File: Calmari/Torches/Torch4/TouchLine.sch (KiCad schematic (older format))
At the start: 18 parts

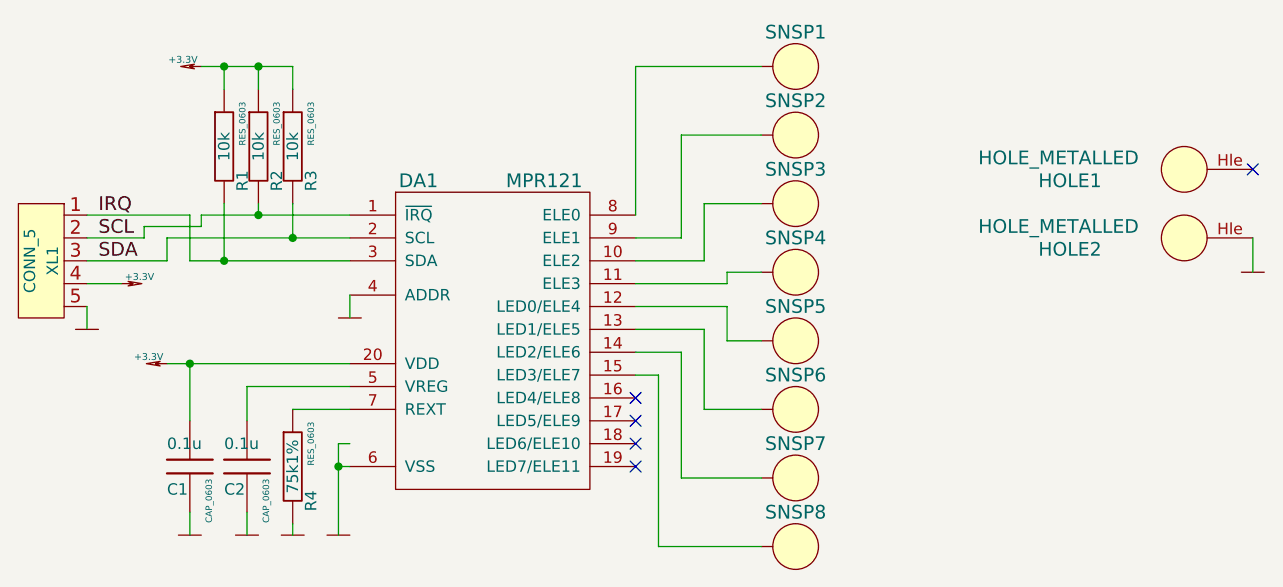
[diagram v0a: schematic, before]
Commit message: 
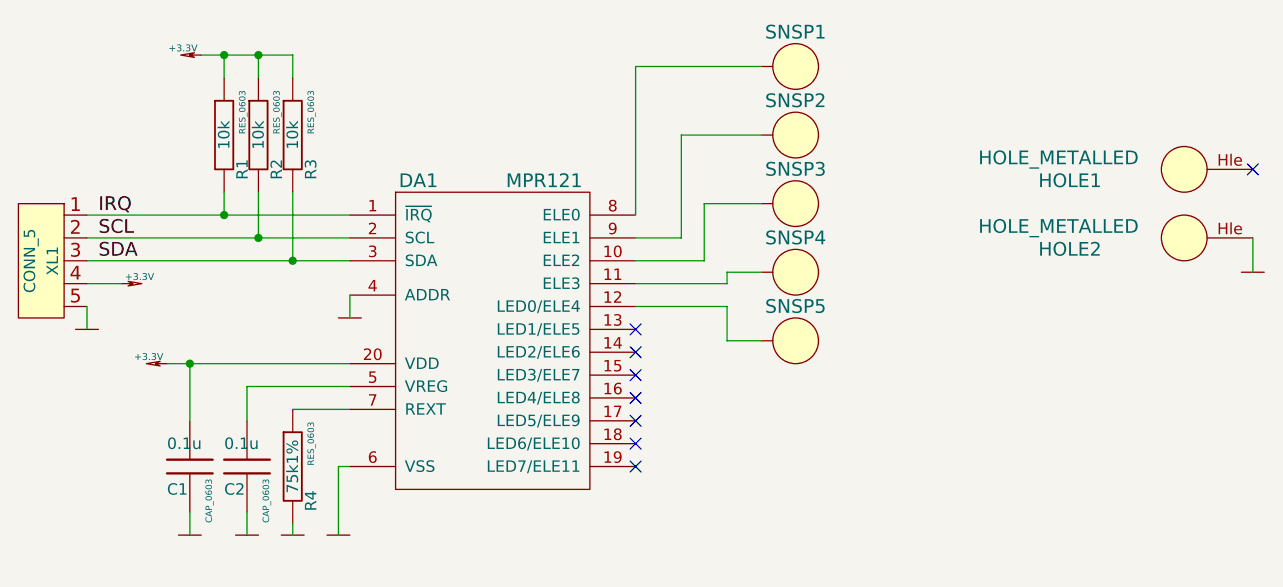
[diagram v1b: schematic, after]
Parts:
- removed SNSP6, SNSP7, SNSP8: SENSORPAD, symbol SENSORPAD
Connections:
- net IRQ: now also DA1.1 (~IRQ); no longer DA1.3 (SDA)
- net SCL: now also DA1.2 (SCL); no longer DA1.1 (~IRQ)
- net SDA: now also DA1.3 (SDA); no longer DA1.2 (SCL)
- no-connect marks 5 -> 8
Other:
- moved on the sheet: R1, R2, R3
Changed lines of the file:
@@
 LIBS:Sensors
 LIBS:Tittar_kl
+LIBS:TouchLine-cache
 EELAYER 27 0
 EELAYER END
@@
 Sheet 1 1
 Title ""
-Date "1 sep 2014"
+Date "15 sep 2014"
 Rev ""
 Comp ""
@@
 L R R3
 U 1 1 54045D60
-P 4750 2400
-F 0 "R3" V 4830 2250 50  0000 C CNN
-F 1 "10k" V 4750 2400 50  0000 C CNN
-F 2 "RES_0603" V 4830 2500 28  0000 C CNN
-F 3 "~" H 4750 2400 60  0000 C CNN
-	1    4750 2400
+P 4750 2350
+F 0 "R3" V 4830 2200 50  0000 C CNN
+F 1 "10k" V 4750 2350 50  0000 C CNN
+F 2 "RES_0603" V 4830 2450 28  0000 C CNN
+F 3 "~" H 4750 2350 60  0000 C CNN
+	1    4750 2350
 	1    0    0    -1
 $EndComp
@@
 L R R2
 U 1 1 54045D81
-P 4600 2400
-F 0 "R2" V 4680 2250 50  0000 C CNN
-F 1 "10k" V 4600 2400 50  0000 C CNN
-F 2 "RES_0603" V 4680 2500 28  0000 C CNN
-F 3 "~" H 4600 2400 60  0000 C CNN
-	1    4600 2400
+P 4600 2350
+F 0 "R2" V 4680 2200 50  0000 C CNN
+F 1 "10k" V 4600 2350 50  0000 C CNN
+F 2 "RES_0603" V 4680 2450 28  0000 C CNN
+F 3 "~" H 4600 2350 60  0000 C CNN
+	1    4600 2350
 	1    0    0    -1
 $EndComp
@@
 L R R1
 U 1 1 54045D87
-P 4450 2400
-F 0 "R1" V 4530 2250 50  0000 C CNN
-F 1 "10k" V 4450 2400 50  0000 C CNN
-F 2 "RES_0603" V 4530 2500 28  0000 C CNN
-F 3 "~" H 4450 2400 60  0000 C CNN
-	1    4450 2400
+P 4450 2350
+F 0 "R1" V 4530 2200 50  0000 C CNN
+F 1 "10k" V 4450 2350 50  0000 C CNN
+F 2 "RES_0603" V 4530 2450 28  0000 C CNN
+F 3 "~" H 4450 2350 60  0000 C CNN
+	1    4450 2350
 	1    0    0    -1
 $EndComp
@@
 L +3.3V #PWR07
 U 1 1 54045E06
-P 4350 2050
-F 0 "#PWR07" H 4350 2010 30  0001 C CNN
-F 1 "+3.3V" H 4430 2080 30  0000 C CNN
-F 2 "~" H 4350 2050 60  0000 C CNN
-F 3 "~" H 4350 2050 60  0000 C CNN
-	1    4350 2050
+P 4350 2000
+F 0 "#PWR07" H 4350 1960 30  0001 C CNN
+F 1 "+3.3V" H 4430 2030 30  0000 C CNN
+F 2 "~" H 4350 2000 60  0000 C CNN
+F 3 "~" H 4350 2000 60  0000 C CNN
+	1    4350 2000
 	-1   0    0    -1
 $EndComp
@@
 NoConn ~ 6250 3500
 $Comp
-L SENSORPAD SNSP5
-U 1 1 540461E0
-P 6950 3250
-F 0 "SNSP5" H 6950 3400 60  0000 C CNN
-F 1 "SENSORPAD" H 6925 3475 60  0001 C CNN
-F 2 "" H 6950 3250 60  0000 C CNN
-F 3 "" H 6950 3250 60  0000 C CNN
-	1    6950 3250
-	1    0    0    -1
-$EndComp
-$Comp
 L SENSORPAD SNSP4
 U 1 1 540461EF
@@
 $EndComp
 $Comp
-L SENSORPAD SNSP6
-U 1 1 5404620D
-P 6950 3550
-F 0 "SNSP6" H 6950 3700 60  0000 C CNN
-F 1 "SENSORPAD" H 6925 3775 60  0001 C CNN
-F 2 "" H 6950 3550 60  0000 C CNN
-F 3 "" H 6950 3550 60  0000 C CNN
-	1    6950 3550
-	1    0    0    -1
-$EndComp
-$Comp
 L SENSORPAD SNSP2
 U 1 1 5404621C
@@
 $EndComp
 $Comp
-L SENSORPAD SNSP7
-U 1 1 5404622B
-P 6950 3850
-F 0 "SNSP7" H 6950 4000 60  0000 C CNN
-F 1 "SENSORPAD" H 6925 4075 60  0001 C CNN
-F 2 "" H 6950 3850 60  0000 C CNN
-F 3 "" H 6950 3850 60  0000 C CNN
-	1    6950 3850
-	1    0    0    -1
-$EndComp
-$Comp
 L SENSORPAD SNSP1
 U 1 1 5404623A
@@
 $EndComp
 $Comp
-L SENSORPAD SNSP8
-U 1 1 54046249
-P 6950 4150
-F 0 "SNSP8" H 6950 4300 60  0000 C CNN
-F 1 "SENSORPAD" H 6925 4375 60  0001 C CNN
-F 2 "" H 6950 4150 60  0000 C CNN
-F 3 "" H 6950 4150 60  0000 C CNN
-	1    6950 4150
-	1    0    0    -1
-$EndComp
-$Comp
 L HOLE_METALLED HOLE1
 U 1 1 54047142
@@
 	1    0    0    -1
 $EndComp
-Wire Wire Line
-	4550 4100 4550 4000
-Wire Wire Line
-	4300 4100 4300 4000
-Wire Wire Line
-	4750 4050 4750 4100
-Wire Wire Line
-	4950 4100 4950 3700
-Wire Wire Line
-	4950 3700 5000 3700
-Wire Wire Line
-	5000 3800 4950 3800
-Connection ~ 4950 3800
-Wire Wire Line
-	4750 3550 5000 3550
-Wire Wire Line
-	5000 3450 4550 3450
-Wire Wire Line
-	4550 3450 4550 3600
-Wire Wire Line
-	4200 3350 5000 3350
-Wire Wire Line
-	4300 3350 4300 3600
-Connection ~ 4300 3350
-Wire Wire Line
-	5000 3150 5000 3050
-Wire Wire Line
-	4450 2150 4450 2050
-Wire Wire Line
-	4350 2050 4750 2050
-Wire Wire Line
-	4750 2050 4750 2150
-Wire Wire Line
-	4600 2150 4600 2050
-Connection ~ 4600 2050
-Connection ~ 4450 2050
-Wire Wire Line
-	3850 3200 3850 3100
-Wire Wire Line
-	3850 3000 4000 3000
-Wire Wire Line
-	6250 3000 6650 3000
-Wire Wire Line
-	6650 3000 6650 2950
-Wire Wire Line
-	6650 2950 6800 2950
-Wire Wire Line
-	6250 3100 6650 3100
-Wire Wire Line
-	6650 3100 6650 3250
-Wire Wire Line
-	6650 3250 6800 3250
-Wire Wire Line
-	6250 3200 6550 3200
-Wire Wire Line
-	6550 3200 6550 3550
-Wire Wire Line
-	6550 3550 6800 3550
-Wire Wire Line
-	6250 3300 6450 3300
-Wire Wire Line
-	6450 3300 6450 3850
-Wire Wire Line
-	6450 3850 6800 3850
-Wire Wire Line
-	6250 3400 6350 3400
-Wire Wire Line
-	6350 3400 6350 4150
-Wire Wire Line
-	6350 4150 6800 4150
-Wire Wire Line
-	6250 2900 6550 2900
-Wire Wire Line
-	6550 2900 6550 2650
-Wire Wire Line
-	6550 2650 6800 2650
-Wire Wire Line
-	6250 2800 6450 2800
-Wire Wire Line
-	6450 2800 6450 2350
-Wire Wire Line
-	6450 2350 6800 2350
-Wire Wire Line
-	6250 2700 6250 2050
-Wire Wire Line
-	6250 2050 6800 2050
-Wire Wire Line
-	8950 2950 8950 2800
-Wire Wire Line
-	5000 2900 4300 2900
-Wire Wire Line
-	4300 2900 4300 2700
-Wire Wire Line
-	4300 2700 3850 2700
-Wire Wire Line
-	5000 2800 4200 2800
-Wire Wire Line
-	4200 2800 4200 2900
-Wire Wire Line
-	4200 2900 3850 2900
-Wire Wire Line
-	3850 2800 4100 2800
-Wire Wire Line
-	4100 2800 4100 2750
-Wire Wire Line
-	4100 2750 4350 2750
-Wire Wire Line
-	4350 2750 4350 2700
-Wire Wire Line
-	4350 2700 5000 2700
-Wire Wire Line
-	4450 2650 4450 2900
-Connection ~ 4450 2900
-Wire Wire Line
-	4600 2650 4600 2700
-Connection ~ 4600 2700
-Wire Wire Line
-	4750 2650 4750 2800
-Connection ~ 4750 2800
 Text Label 3900 2700 0    60   ~ 0
 IRQ
@@
 Text Label 3900 2900 0    60   ~ 0
 SDA
+Wire Wire Line
+	4550 4100 4550 4000
+Wire Wire Line
+	4300 4100 4300 4000
+Wire Wire Line
+	4750 4050 4750 4100
+Wire Wire Line
+	5000 3800 4950 3800
+Wire Wire Line
+	4750 3550 5000 3550
+Wire Wire Line
+	5000 3450 4550 3450
+Wire Wire Line
+	4550 3450 4550 3600
+Wire Wire Line
+	4200 3350 5000 3350
+Wire Wire Line
+	4300 3350 4300 3600
+Connection ~ 4300 3350
+Wire Wire Line
+	5000 3150 5000 3050
+Wire Wire Line
+	4450 2100 4450 2000
+Wire Wire Line
+	4350 2000 4750 2000
+Wire Wire Line
+	4750 2000 4750 2100
+Wire Wire Line
+	4600 2100 4600 2000
+Connection ~ 4600 2000
+Connection ~ 4450 2000
+Wire Wire Line
+	3850 3200 3850 3100
+Wire Wire Line
+	3850 3000 4000 3000
+Wire Wire Line
+	6250 3000 6650 3000
+Wire Wire Line
+	6650 3000 6650 2950
+Wire Wire Line
+	6650 2950 6800 2950
+Wire Wire Line
+	6250 2900 6550 2900
+Wire Wire Line
+	6550 2900 6550 2650
+Wire Wire Line
+	6550 2650 6800 2650
+Wire Wire Line
+	6250 2800 6450 2800
+Wire Wire Line
+	6450 2800 6450 2350
+Wire Wire Line
+	6450 2350 6800 2350
+Wire Wire Line
+	6250 2700 6250 2050
+Wire Wire Line
+	6250 2050 6800 2050
+Wire Wire Line
+	8950 2950 8950 2800
+Wire Wire Line
+	3850 2700 5000 2700
+Wire Wire Line
+	3850 2900 5000 2900
+Wire Wire Line
+	3850 2800 5000 2800
+Wire Wire Line
+	4750 2600 4750 2900
+Connection ~ 4750 2900
+Wire Wire Line
+	4600 2600 4600 2800
+Connection ~ 4600 2800
+Wire Wire Line
+	4450 2600 4450 2700
+Connection ~ 4450 2700
+$Comp
+L SENSORPAD SNSP5
+U 1 1 54172112
+P 6950 3250
+F 0 "SNSP5" H 6950 3400 60  0000 C CNN
+F 1 "SENSORPAD" H 6925 3475 60  0001 C CNN
+F 2 "" H 6950 3250 60  0000 C CNN
+F 3 "" H 6950 3250 60  0000 C CNN
+	1    6950 3250
+	1    0    0    -1
+$EndComp
+Wire Wire Line
+	6800 3250 6650 3250
+Wire Wire Line
+	6650 3250 6650 3100
+Wire Wire Line
+	6650 3100 6250 3100
+NoConn ~ 6250 3200
+NoConn ~ 6250 3300
+NoConn ~ 6250 3400
+Wire Wire Line
+	4950 3800 4950 4100
 $EndSCHEMATC
